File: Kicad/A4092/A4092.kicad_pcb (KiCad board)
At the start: 4 copper layers, 175.6 x 122.1 mm, 133 parts, among them CN1 Zorro3, J1 5749721-7, J2 5749721-7, J3 TO-LED, J4 TO-MB, J5 TO-A3000-LED, J6 TO-A3000-MB, J8 Conn_01x06_Pin, U1 SN74ABT16543DGGR, U10 DS21S07A, U11 DS21S07A, U12 DS21S07A, U13 W25X40CLSN, U2 SN74ABT16543DGGR, U3 SN74ABT16543DGGR, U4 SN74ABT16543DGGR, U5 74LVC07APW_118, U6 SN74ABT16245ADGGR, U7 AMS1117-3.3, U8 XC95144XL-TQ144, U9 LSI53C770 SCSI Host Controller, Y1 Abracon ACO-50MHz, Y2 Abracon ACO-40MHz

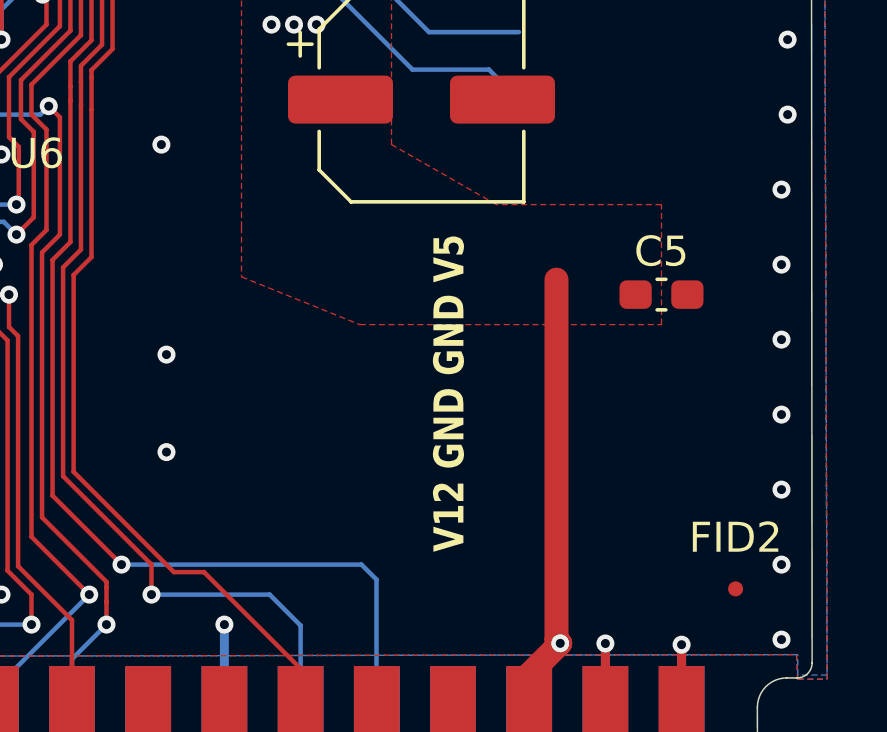
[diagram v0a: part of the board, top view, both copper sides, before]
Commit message: Adjust back side silkscreen on PCB
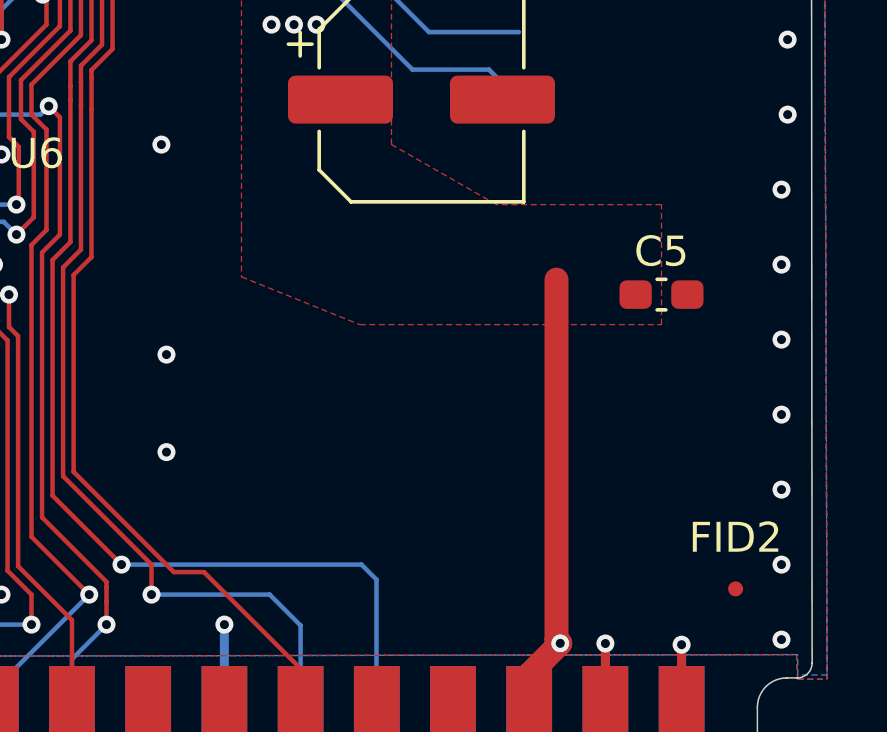
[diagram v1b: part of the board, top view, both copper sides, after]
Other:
- board text added: "PCB: Monse Almaraz Schematics: Stefan Reinauer Special thanks to: Chris Hooper, Salih Albayrak, Dorken, Eduardo Michel, Matt Harlum Original A4091: DH/SS/GB/FISH"
- board text added: "REV A 2026/01/09"
- board text removed: "PCB: Monse Almaraz Schematics: Stefan Reinauer Special thanks to: Chris Hooper, Salih Albayrak, Eduardo Michel Matt Harlum, Dorken Original A4091: DH/SS/GB/FISH"
- board text removed: "REV A 2025/06/01"
- board text removed: "V12 GND GND V5"

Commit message: Undo last two PCB changes
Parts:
- removed R131, R132, R133, R134: 33, Resistor_SMD:R_0603_1608Metric
- removed R7: 0, Resistor_SMD:R_0603_1608Metric
- removed R8: 22, Resistor_SMD:R_0603_1608Metric
- moved C8 51.9 mm to (110.0, 114.5)
- moved R6 50.2 mm to (113.0, 117.0), turned to 90 degrees
- moved R5 46.1 mm to (113.0, 120.0), turned to 90 degrees
- moved Y2 44.1 mm to (110.0, 118.5)
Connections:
- R130 pad 1: Net-(U13-~{CS}) -> SPI_CS_n
- R4 pad 2: BCLK_FULL -> BCLK
- U13 pad 1: Net-(U13-~{CS}) -> SPI_CS_n
- U13 pad 2: Net-(U13-DO/IO_{1}) -> SPI_MISO
- U13 pad 5: Net-(U13-DI/IO_{0}) -> SPI_MOSI
- U13 pad 6: Net-(U13-CLK) -> SPI_CLK
- U8 pad 30: BCLK_FULL -> BCLK
- U8 pad 49: unconnected-(U8-P49-Pad49) -> PLD_SID
- U8 pad 91: BCLK_HALF -> unconnected-(U8-P91-Pad91)
- U9 pad 119: GND -> (no net)
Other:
- board text added: "PCB: Monse Almaraz Schematics: Stefan Reinauer Special thanks to: Chris Hooper, Salih Albayrak, Eduardo Michel Matt Harlum, Dorken Original A4091: DH/SS/GB/FISH"
- board text added: "REV A 2025/06/01"
- board text added: "V12 GND GND V5"
- board text removed: "PCB: Monse Almaraz Schematics: Stefan Reinauer Special thanks to: Chris Hooper, Salih Albayrak, Dorken, Eduardo Michel, Matt Harlum Original A4091: DH/SS/GB/FISH"
- board text removed: "REV A 2026/01/09"

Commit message: Update PCB from Schematic
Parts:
- added R131: 33, Resistor_SMD:R_0603_1608Metric, F.Cu at (80.1, 162.4)
- added R132: 33, Resistor_SMD:R_0603_1608Metric, F.Cu at (80.1, 164.9)
- added R133: 33, Resistor_SMD:R_0603_1608Metric, F.Cu at (80.1, 167.4)
- added R134: 33, Resistor_SMD:R_0603_1608Metric, F.Cu at (80.1, 169.9)
- added R7: 0, Resistor_SMD:R_0603_1608Metric, F.Cu at (80.1, 157.4)
- added R8: 22, Resistor_SMD:R_0603_1608Metric, F.Cu at (80.1, 159.9)
- moved C8 51.9 mm to (84.3, 159.7)
- moved R6 50.2 mm to (80.1, 154.9), turned to 0 degrees
- moved R5 46.1 mm to (80.1, 152.4), turned to 0 degrees
- moved Y2 44.1 mm to (84.9, 154.8)
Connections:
- R130 pad 1: SPI_CS_n -> Net-(U13-~{CS})
- R4 pad 2: BCLK -> BCLK_FULL
- U13 pad 1: SPI_CS_n -> Net-(U13-~{CS})
- U13 pad 2: SPI_MISO -> Net-(U13-DO/IO_{1})
- U13 pad 5: SPI_MOSI -> Net-(U13-DI/IO_{0})
- U13 pad 6: SPI_CLK -> Net-(U13-CLK)
- U8 pad 30: BCLK -> BCLK_FULL
- U8 pad 49: PLD_SID -> unconnected-(U8-P49-Pad49)
- U8 pad 91: unconnected-(U8-P91-Pad91) -> BCLK_HALF
- U9 pad 119: (no net) -> GND
